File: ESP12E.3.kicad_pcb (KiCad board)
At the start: 2 copper layers, 32.4 x 33.7 mm, 30 parts, among them Q1 MOSFET-NREFLOW, U1 SPX3819M5-L-3-3, X1 ESP-12

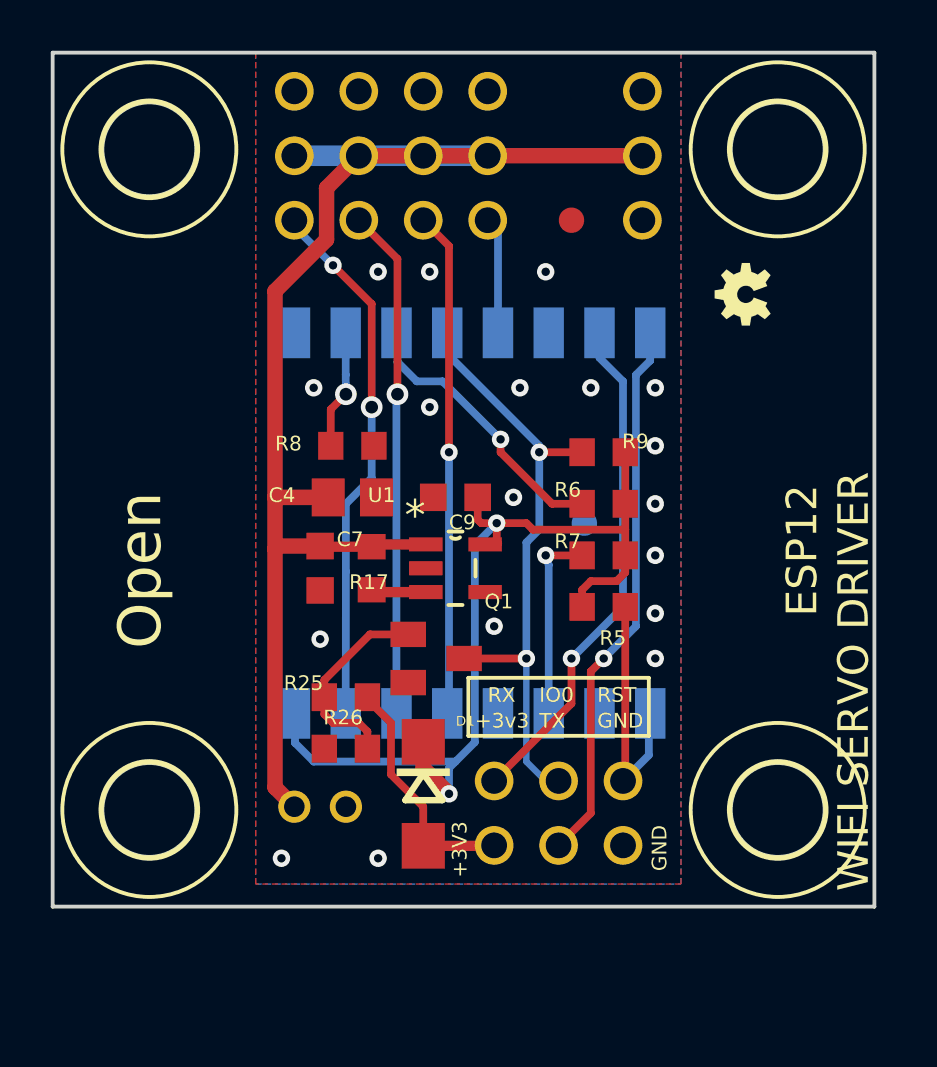
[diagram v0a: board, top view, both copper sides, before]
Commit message: Update to net assignments and part updates.
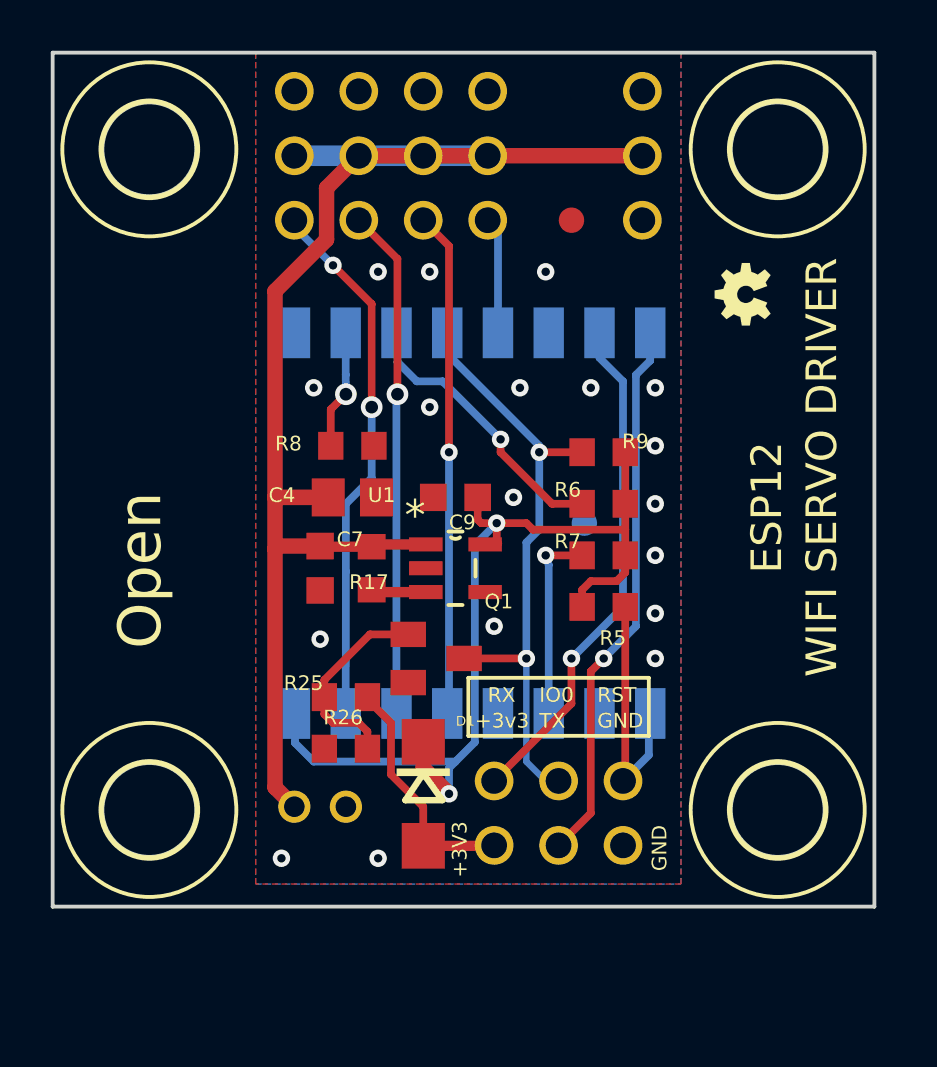
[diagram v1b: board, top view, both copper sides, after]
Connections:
- net Net-(X1-Pad14) renamed /GPIO4
- net Net-(X1-Pad15) renamed /RXD
- net Net-(X1-Pad16) renamed /TXD
- net Net-(X1-Pad2) renamed /ADC
- net Net-(X1-Pad4) renamed /GPIO16
- JP1 pad 1: /GPIO5 -> (no net)
- JP1 pad 2: VCC -> (no net)
- JP1 pad 3: GND -> (no net)
- JP10 pad 1: GND -> (no net)
- JP10 pad 2: VCC -> (no net)
- JP10 pad 3: GND -> (no net)
- JP11 pad 1: Net-(JP11-Pad1) -> (no net)
- JP11 pad 2: Net-(JP11-Pad2) -> (no net)
- JP11 pad 3: Net-(JP11-Pad3) -> (no net)
- JP2 pad 1: /GPIO14 -> (no net)
- JP2 pad 2: VCC -> (no net)
- JP2 pad 3: GND -> (no net)
- JP3 pad 1: /GPIO12 -> (no net)
- JP3 pad 2: VCC -> (no net)
- JP3 pad 3: GND -> (no net)
- JP4 pad 1: /GPIO13 -> (no net)
- JP4 pad 2: VCC -> (no net)
- JP4 pad 3: GND -> (no net)
- JP9 pad 1: Net-(JP9-Pad1) -> (no net)
- JP9 pad 2: Net-(JP9-Pad2) -> (no net)
- JP9 pad 3: Net-(JP9-Pad3) -> (no net)
- X1 pad 1: Net-(X1-Pad1) -> /RESET
- X1 pad 10: Net-(X1-Pad10) -> /GPIO15
- X1 pad 11: Net-(X1-Pad11) -> /GPIO2
- X1 pad 12: Net-(X1-Pad12) -> /GPIO0
- X1 pad 13: Net-(X1-Pad13) -> /GPIO5
- X1 pad 3: Net-(X1-Pad3) -> /CH_PD
- X1 pad 5: Net-(X1-Pad5) -> /GPIO14
- X1 pad 6: Net-(X1-Pad6) -> /GPIO12
- X1 pad 7: Net-(X1-Pad7) -> /GPIO13
- X1 pad 8: VCC -> +3V3
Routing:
- net VCC: track 93.8 -> 54.5 mm, vias 2 -> 0
- net +3V3: track 0.00 -> 39.2 mm, vias 0 -> 2
- net Net-(JP9-Pad2): track 24.4 -> 0.51 mm, vias 2 -> 0
- net /GPIO0: track 0.00 -> 23.9 mm, vias 0 -> 2
- net Net-(JP11-Pad2): track 21.8 -> 0.00 mm, vias 1 -> 0
- net /TXD: track 0.00 -> 21.8 mm, vias 0 -> 1
- net Net-(JP9-Pad1): track 20.8 -> 0.00 mm, vias 1 -> 0
- net /RXD: track 0.00 -> 20.8 mm, vias 0 -> 1
- net Net-(JP9-Pad3): track 10.00 -> 0.00 mm
- net /RESET: track 0.00 -> 10.00 mm
- net Net-(JP11-Pad1): track 9.71 -> 0.03 mm
- net /P3V3: track 0.00 -> 9.69 mm
- net (no net): track 0.00 -> 1.44 mm
- net /GPIO14: track 19.9 -> 18.5 mm
- net Net-(JP11-Pad3): vias 18 -> 0
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- added copper zone on B.Cu, net GND
- added copper zone on F.Cu, net GND
- removed copper zone on B.Cu, net Net-(JP11-Pad3)
- removed copper zone on F.Cu, net Net-(JP11-Pad3)
